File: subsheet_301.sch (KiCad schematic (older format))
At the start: 19 parts, among them J301 DB-19S ACSI Port, U302 74LS245_PHY, U306 74LS74_PHY, U307 74LS244_PHY

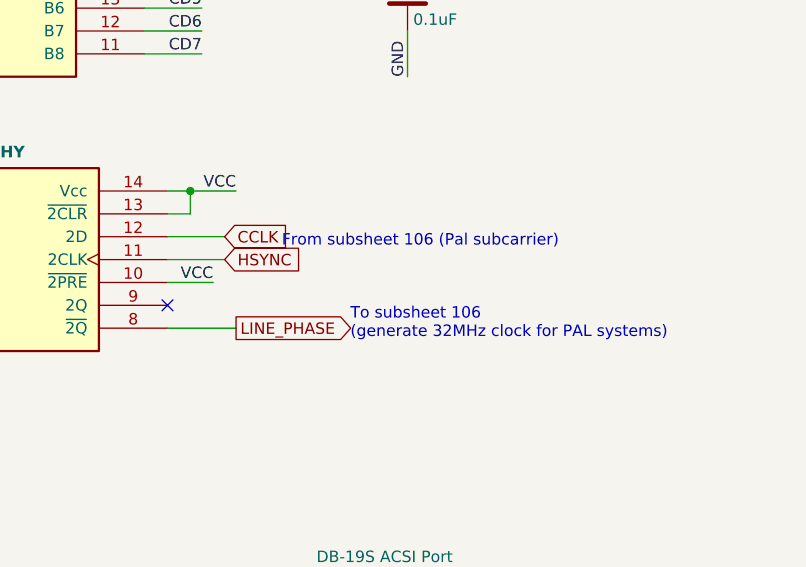
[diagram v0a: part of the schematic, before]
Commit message: Delete circuitry related to PAL/NTSC and modulator
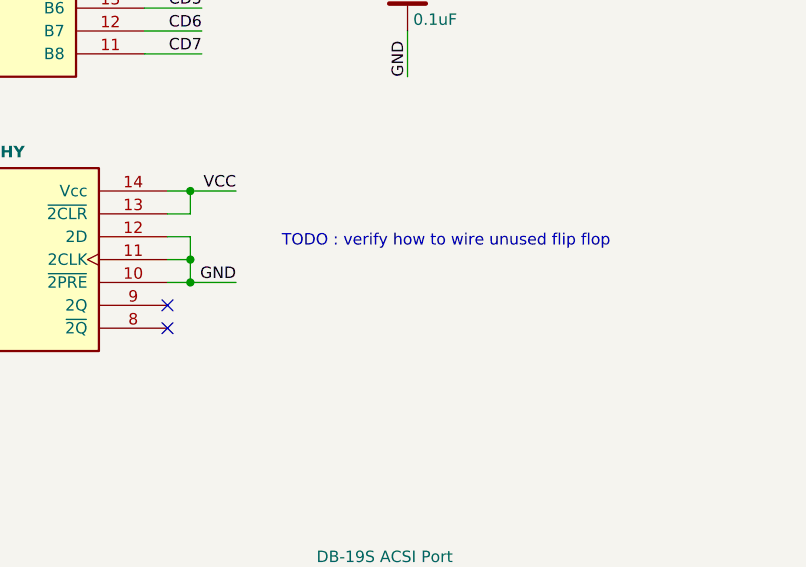
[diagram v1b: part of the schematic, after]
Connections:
- net CCLK is gone; now on net GND: U306.12 (2D)
- net HSYNC is gone; now on net GND: U306.11 (2CLK)
- net GND: now also U306.10 (~2PRE~)
- net VCC: no longer U306.10 (~2PRE~)
- net LINE_PHASE: no longer names the net of U306.8 (~2Q~)
- no-connect marks 6 -> 7
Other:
- note added: "TODO : verify how to wire unused flip flop"
- note removed: "From subsheet 106 (Pal subcarrier)"
- note removed: "To subsheet 106 \n(generate 32MHz clock for PAL systems)"
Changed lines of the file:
@@
 Text Label 5000 4600 2    50   ~ 0
 VCC
-Text Label 4900 5000 2    50   ~ 0
-VCC
-Text GLabel 4950 4800 2    50   Input ~ 0
-CCLK
-Text GLabel 4950 4900 2    50   Input ~ 0
-HSYNC
-Text GLabel 5000 5200 2    50   Output ~ 0
-LINE_PHASE
 Wire Wire Line
 	3100 4900 3300 4900
@@
 Wire Wire Line
 	4800 4600 5000 4600
-Wire Wire Line
-	4700 4800 4950 4800
-Wire Wire Line
-	4700 4900 4950 4900
-Wire Wire Line
-	4700 5000 4900 5000
-Wire Wire Line
-	4700 5200 5000 5200
 Text Notes 5200 4850 0    50   ~ 0
-From subsheet 106 (Pal subcarrier)
-Text Notes 5500 5250 0    50   ~ 0
-To subsheet 106 \n(generate 32MHz clock for PAL systems)
+TODO : verify how to wire unused flip flop
 Text Label 3750 6000 2    50   ~ 0
 acsi_1
@@
 Wire Wire Line
 	5650 8600 5650 8400
+NoConn ~ 4700 5200
+Text Label 5000 5000 2    50   ~ 0
+GND
+Wire Wire Line
+	4700 4800 4800 4800
+Wire Wire Line
+	4700 5000 4800 5000
+Connection ~ 4800 5000
+Wire Wire Line
+	4800 5000 5000 5000
+Wire Wire Line
+	4800 4800 4800 4900
+Wire Wire Line
+	4700 4900 4800 4900
+Connection ~ 4800 4900
+Wire Wire Line
+	4800 4900 4800 5000
 $EndSCHEMATC

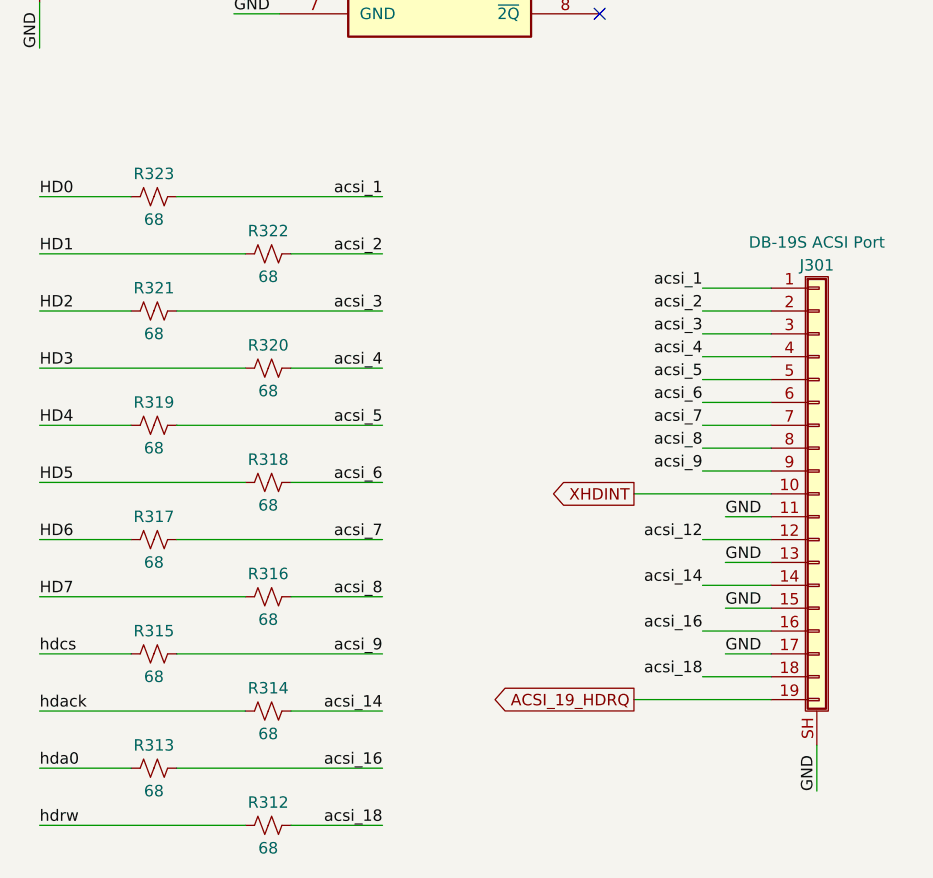
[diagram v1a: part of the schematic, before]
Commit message: Resolves #1 : Use 4-resistor packs wherever it is possible
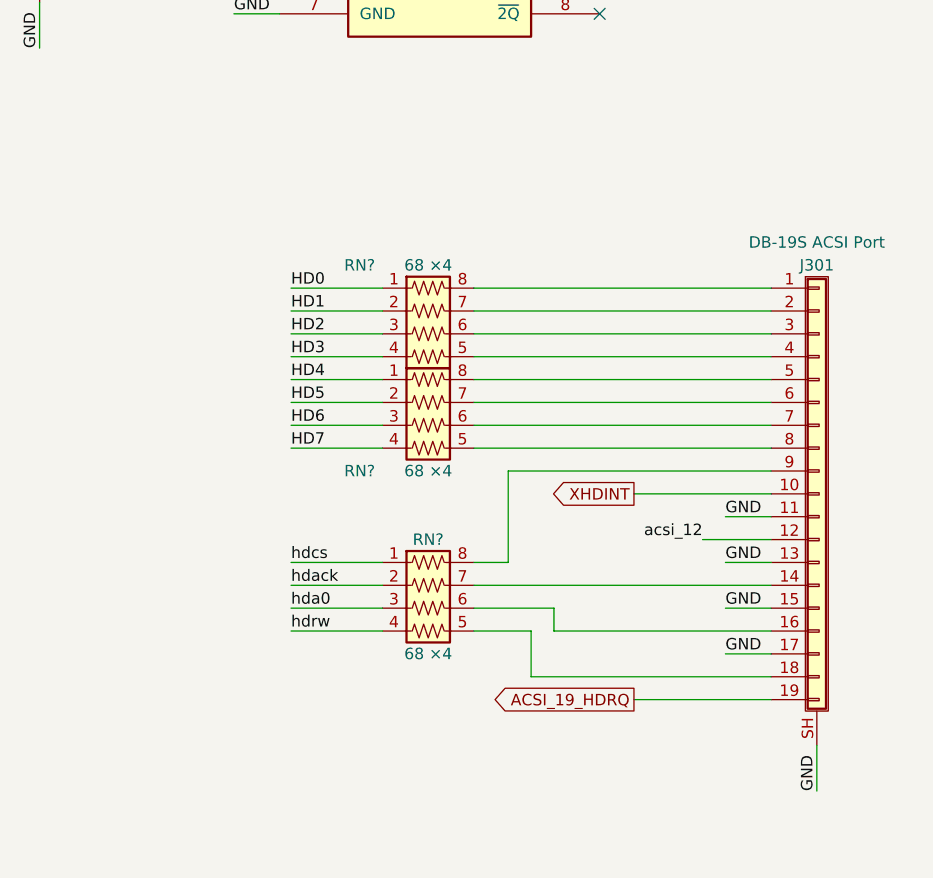
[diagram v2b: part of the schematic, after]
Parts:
- removed R312, R313, R314, R315, R316, R317, R318, R319, R320, R321, R322, R323: 68, commons_passives_THT:Passive_THT_resistor_W2.54mm_L12.70mm, symbol Device:R_Small_US
- added RN? (x3): 68 ×4, symbol custom_passives:R_Pack04_US
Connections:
- net HD0: now also RN?.1 (R1.1)
- net HD1: now also RN?.2 (R2.1)
- net HD2: now also RN?.3 (R3.1)
- net HD3: now also RN?.4 (R4.1)
- net HD4: now also RN?.1 (R1.1)
- net HD5: now also RN?.2 (R2.1)
- net HD6: now also RN?.3 (R3.1)
- net HD7: now also RN?.4 (R4.1)
- net hda0: now also RN?.3 (R3.1)
- net hdack: now also RN?.2 (R2.1)
- net hdcs: now also RN?.1 (R1.1)
- net hdrw: now also RN?.4 (R4.1)
- net acsi_1: no longer names the net of J301.1 (Pin_1)
- net acsi_1: now also RN?.8 (R1.2)
- net acsi_14: no longer names the net of J301.14 (Pin_14)
- net acsi_14: now also RN?.7 (R2.2)
- net acsi_16: no longer names the net of J301.16 (Pin_16)
- net acsi_16: now also RN?.6 (R3.2)
- net acsi_18: no longer names the net of J301.18 (Pin_18)
- net acsi_18: now also RN?.5 (R4.2)
- net acsi_2: no longer names the net of J301.2 (Pin_2)
- net acsi_2: now also RN?.7 (R2.2)
- net acsi_3: no longer names the net of J301.3 (Pin_3)
- net acsi_3: now also RN?.6 (R3.2)
- net acsi_4: no longer names the net of J301.4 (Pin_4)
- net acsi_4: now also RN?.5 (R4.2)
- net acsi_5: no longer names the net of J301.5 (Pin_5)
- net acsi_5: now also RN?.8 (R1.2)
- net acsi_6: no longer names the net of J301.6 (Pin_6)
- net acsi_6: now also RN?.7 (R2.2)
- net acsi_7: no longer names the net of J301.7 (Pin_7)
- net acsi_7: now also RN?.6 (R3.2)
- net acsi_8: no longer names the net of J301.8 (Pin_8)
- net acsi_8: now also RN?.5 (R4.2)
- net acsi_9: no longer names the net of J301.9 (Pin_9)
- net acsi_9: now also RN?.8 (R1.2)

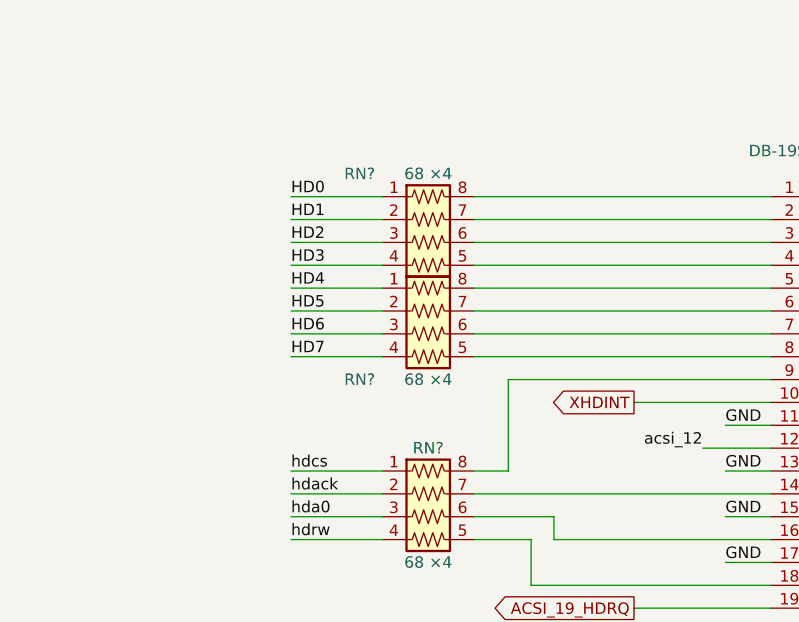
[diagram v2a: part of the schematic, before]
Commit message: annotate resistor networks and mark unused pins as unconnected
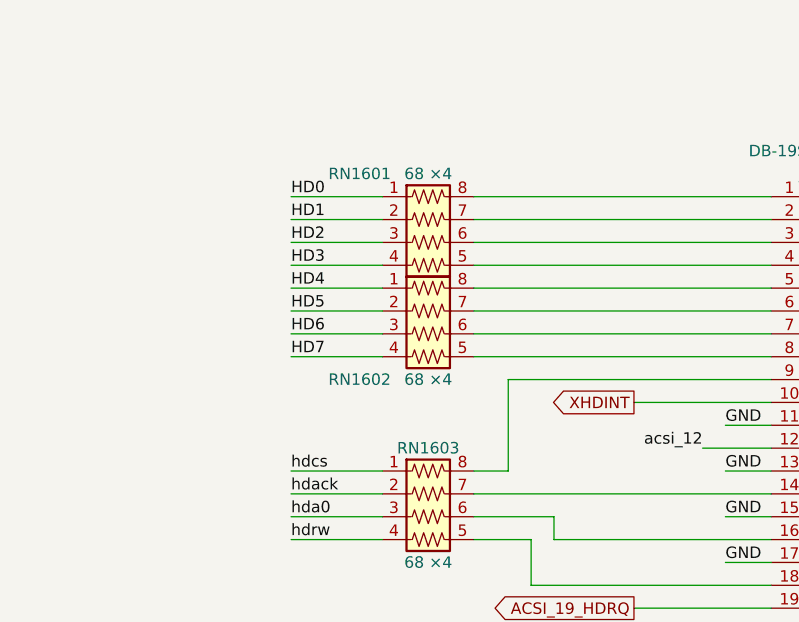
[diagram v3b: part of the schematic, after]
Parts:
- gave numbers to parts that had none: 3
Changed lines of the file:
@@
 	4800 4900 4800 5000
 $Comp
-L custom_passives:R_Pack04_US RN?
+L custom_passives:R_Pack04_US RN1601
 U 1 1 61FF226E
 P 3950 6600
-F 0 "RN?" V 3650 6300 50  0000 C CNN
+F 0 "RN1601" V 3650 6300 50  0000 C CNN
 F 1 "68 ×4" V 3650 6600 50  0000 C CNN
 F 2 "" V 4225 6600 50  0001 C CNN
@@
 $EndComp
 $Comp
-L custom_passives:R_Pack04_US RN?
+L custom_passives:R_Pack04_US RN1602
 U 1 1 61FF320D
 P 3950 7000
-F 0 "RN?" V 4150 6700 50  0000 C CNN
+F 0 "RN1602" V 4150 6700 50  0000 C CNN
 F 1 "68 ×4" V 4150 7000 50  0000 C CNN
 F 2 "" V 4225 7000 50  0001 C CNN
@@
 $EndComp
 $Comp
-L custom_passives:R_Pack04_US RN?
+L custom_passives:R_Pack04_US RN1603
 U 1 1 61FF4DF9
 P 3950 7800
-F 0 "RN?" V 3650 7800 50  0000 C CNN
+F 0 "RN1603" V 3650 7800 50  0000 C CNN
 F 1 "68 ×4" V 4150 7800 50  0000 C CNN
 F 2 "" V 4225 7800 50  0001 C CNN

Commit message: Resolves #7 : Assign SMD footprints to resistors pack
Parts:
- RN1601, RN1602, RN1603: footprint (none) -> Resistor_SMD:R_Array_Convex_4x0603
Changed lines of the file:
@@
 F 0 "RN1601" V 3650 6300 50  0000 C CNN
 F 1 "68 ×4" V 3650 6600 50  0000 C CNN
-F 2 "" V 4225 6600 50  0001 C CNN
+F 2 "Resistor_SMD:R_Array_Convex_4x0603" V 4225 6600 50  0001 C CNN
 F 3 "~" H 3950 6600 50  0001 C CNN
 	1    3950 6600
@@
 F 0 "RN1602" V 4150 6700 50  0000 C CNN
 F 1 "68 ×4" V 4150 7000 50  0000 C CNN
-F 2 "" V 4225 7000 50  0001 C CNN
+F 2 "Resistor_SMD:R_Array_Convex_4x0603" V 4225 7000 50  0001 C CNN
 F 3 "~" H 3950 7000 50  0001 C CNN
 	1    3950 7000
@@
 F 0 "RN1603" V 3650 7800 50  0000 C CNN
 F 1 "68 ×4" V 4150 7800 50  0000 C CNN
-F 2 "" V 4225 7800 50  0001 C CNN
+F 2 "Resistor_SMD:R_Array_Convex_4x0603" V 4225 7800 50  0001 C CNN
 F 3 "~" H 3950 7800 50  0001 C CNN
 	1    3950 7800

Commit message: Resolves #8 : Assign 1206 hand-solder footprints to non polarized capacitors
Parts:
- C303, C306, C307: footprint commons_passives_THT:Passive_THT_capacitor_mlcc_W2.54mm_L7.62mm -> Capacitor_SMD:C_1206_3216Metric_Pad1.33x1.80mm_HandSolder
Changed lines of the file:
@@
 F 0 "C303" H 5775 2350 50  0000 L CNN
 F 1 "0.1uF" H 5775 2150 50  0000 L CNN
-F 2 "commons_passives_THT:Passive_THT_capacitor_mlcc_W2.54mm_L7.62mm" H 5788 2100 50  0001 C CNN
+F 2 "Capacitor_SMD:C_1206_3216Metric_Pad1.33x1.80mm_HandSolder" H 5788 2100 50  0001 C CNN
 F 3 "~" H 5750 2250 50  0001 C CNN
 	1    5750 2250
@@
 F 0 "C306" H 5775 3850 50  0000 L CNN
 F 1 "0.1uF" H 5775 3650 50  0000 L CNN
-F 2 "commons_passives_THT:Passive_THT_capacitor_mlcc_W2.54mm_L7.62mm" H 5788 3600 50  0001 C CNN
+F 2 "Capacitor_SMD:C_1206_3216Metric_Pad1.33x1.80mm_HandSolder" H 5788 3600 50  0001 C CNN
 F 3 "~" H 5750 3750 50  0001 C CNN
 	1    5750 3750
@@
 F 0 "C307" H 2275 5100 50  0000 L CNN
 F 1 "0.1uF" H 2275 4900 50  0000 L CNN
-F 2 "commons_passives_THT:Passive_THT_capacitor_mlcc_W2.54mm_L7.62mm" H 2288 4850 50  0001 C CNN
+F 2 "Capacitor_SMD:C_1206_3216Metric_Pad1.33x1.80mm_HandSolder" H 2288 4850 50  0001 C CNN
 F 3 "~" H 2250 5000 50  0001 C CNN
 	1    2250 5000
